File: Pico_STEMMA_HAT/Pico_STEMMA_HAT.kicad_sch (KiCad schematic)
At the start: 46 parts, among them J1 Conn_01x20_Socket, J2 Conn_01x20_Socket, J3 SDCARD_MODULE, U1 Neopixel

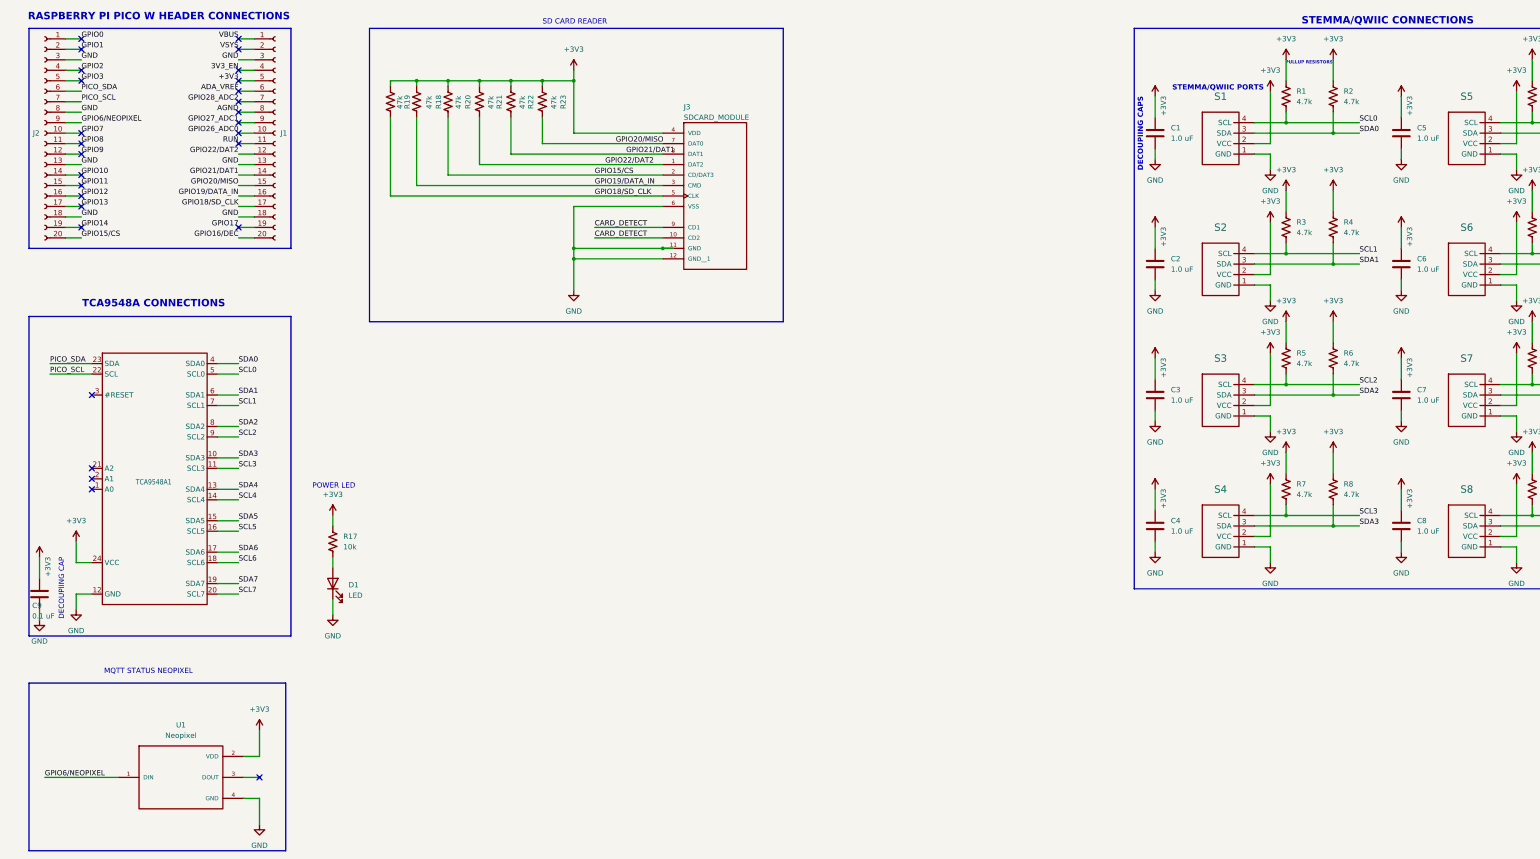
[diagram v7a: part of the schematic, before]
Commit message: Fix STEMMA GND Nets
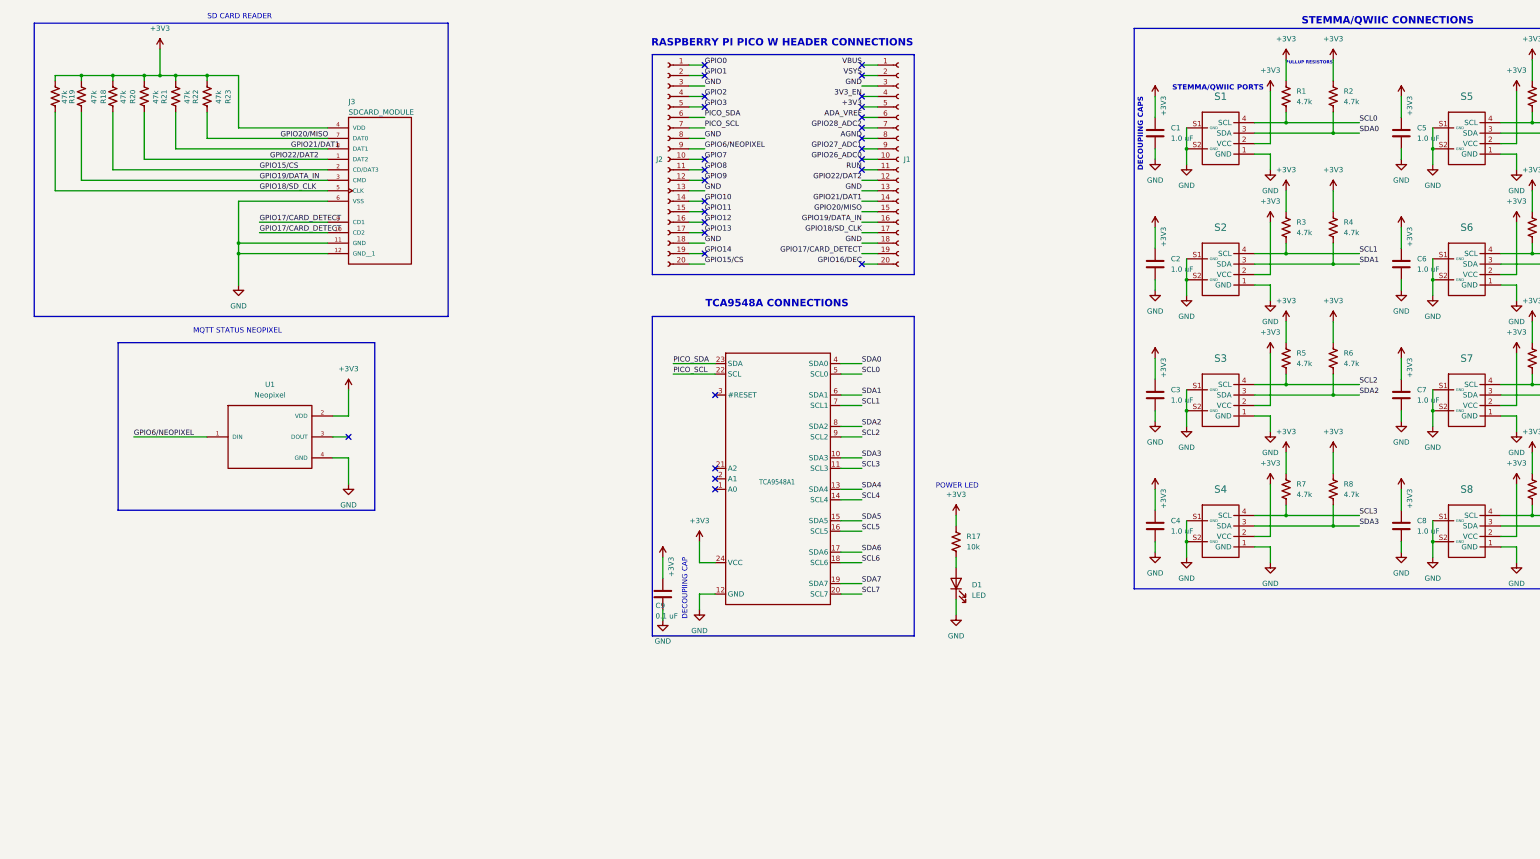
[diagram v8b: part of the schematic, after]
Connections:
- net GPIO17 is gone; now on net GPIO17/CARD_DETECT: J1.19 (Pin_19)
- net GND: now also S1.S1 (GND), S1.S2 (GND), S2.S1 (GND), S2.S2 (GND), S3.S1 (GND), S3.S2 (GND), S4.S1 (GND), S4.S2 (GND), S5.S1 (GND), S5.S2 (GND), S6.S1 (GND), S6.S2 (GND), S7.S1 (GND), S7.S2 (GND), S8.S1 (GND), S8.S2 (GND)
- net CARD_DETECT renamed GPIO17/CARD_DETECT
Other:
- moved on the sheet: C9, D1, J1, J2, J3, R17, R18, R19, R20, R21, R22, R23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
